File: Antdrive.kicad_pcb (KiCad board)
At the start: 2 copper layers, 29 x 32 mm, 27 parts, among them J1 Conn_01x06, J2 Conn_01x03, M1 Conn_01x02, M2 Conn_01x02, Q1 MMBT3904, U2 STM32F030F4Px, U3 DRV8848, U5 HT75xx-1-SOT89

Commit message: Fix auto reset circuits
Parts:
- removed mouse-bite-2mm-slot: VAL**, MountingEquipment:mouse-bite-2mm-slot
- C4: value 0.1u -> 2.2u
- R6: value 1k -> 680
- R7: value 1k -> 10k
- TP1, TP2, TP3: footprint TestPoint:TestPoint_Pad_D1.0mm -> TestPoint:TestPoint_Pad_D2.0mm
- moved TP2 3.32 mm to (158.0, 61.2)
- moved TP1 3.01 mm to (155.1, 61.2)
- moved G*** 0.14 mm to (163.4, 52.1)
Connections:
- C4 pad 1: DTR -> CTS
- R6 pad 1: DTR -> CTS
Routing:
- net DTR: track 20.9 -> 0.00 mm, vias 1 -> 0
- net CTS: track 28.1 -> 36.7 mm
- net BOOT: track 44.6 -> 51.1 mm
- net !RST: track 32.6 -> 33.9 mm
- net !SLEEP: track 34.1 -> 32.7 mm

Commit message: PCB updated
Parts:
- removed G***: LOGO, Symbol:lime_5mm
- removed TP3: Conn_01x01, TestPoint:TestPoint_Pad_D2.0mm
- added J3: Conn_01x03, Connector_PinHeader_2.54mm:PinHeader_1x03_P2.54mm_Vertical, F.Cu at (179.2, 55.2)
- added JP1: SolderJumper_3_Open, Jumper:SolderJumper-3_P1.3mm_Open_Pad1.0x1.5mm_NumberLabels, B.Cu at (176.5, 41.3)
- added JP2: SolderJumper_3_Open, Jumper:SolderJumper-3_P1.3mm_Open_Pad1.0x1.5mm_NumberLabels, B.Cu at (175.9, 54.6)
- added LOGO1: TestPoint, Symbol:lime_5mm, B.Cu at (161.2, 48.8)
- added U1: HT75xx-1-SOT89, Package_TO_SOT_SMD:SOT-89-3, F.Cu at (158.0, 53.6)
- moved BAT1 25.7 mm to (152.4, 46.6)
- moved R6 22.4 mm to (174.6, 53.5), turned to 0 degrees
- moved C4 21.2 mm to (174.6, 51.7)
- moved R4 18.0 mm to (175.6, 40.1), turned to 180 degrees
- moved TP2 16.7 mm to (171.6, 51.4)
- moved R7 16.3 mm to (171.3, 55.1)
- moved TP1 16.2 mm to (168.0, 51.4)
- moved C3 15.9 mm to (156.7, 40.0)
- moved J2 15.2 mm to (179.2, 40.5), turned to 0 degrees
- moved D1 15.1 mm to (174.9, 42.5), turned to 270 degrees
- moved D2 14.9 mm to (171.4, 53.5), turned to 0 degrees
- moved R3 14.7 mm to (167.9, 50.3)
- moved R1 13.7 mm to (171.3, 51.7), turned to 180 degrees
- moved C1 11.4 mm to (160.8, 50.8), turned to 180 degrees
- moved C2 11.3 mm to (159.4, 49.4), turned to 180 degrees
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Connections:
- J2 pad 2: +3V3 -> Net-(J2-Pad2)
- U2 pad 10: !SLEEP -> SERVO
- U2 pad 12: LED -> BIN1
- U2 pad 13: SERVO -> AIN1
- U2 pad 14: Net-(U2-Pad14) -> PPM
- U2 pad 19: PPM -> Net-(U2-Pad19)
- U2 pad 6: AIN1 -> LED
- U2 pad 7: AIN2 -> !SLEEP
- U2 pad 8: BIN2 -> AIN2
- U2 pad 9: BIN1 -> BIN2
- U3 pad 5: Net-(M2-Pad2) -> Net-(M2-Pad1)
- U3 pad 7: Net-(M2-Pad1) -> Net-(M2-Pad2)
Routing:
- net +BATT: track 24.4 -> 69.0 mm, vias 0 -> 3
- net +5V: track 0.00 -> 34.2 mm, vias 0 -> 2
- net BOOT: track 51.1 -> 20.6 mm, vias 5 -> 2
- net SERVO: track 39.4 -> 16.4 mm, vias 1 -> 2
- net !FAULT: track 31.2 -> 18.3 mm, vias 2 -> 0
- net !SLEEP: track 32.7 -> 43.9 mm, vias 2 -> 4
- net AIN1: track 8.31 -> 16.9 mm
- net LED: track 4.23 -> 10.9 mm, vias 0 -> 2
- net +3V3: track 71.3 -> 64.6 mm, vias 6 -> 4
- net RX: track 21.2 -> 14.7 mm
- net AIN2: track 8.31 -> 14.8 mm
- net CTS: track 36.7 -> 30.5 mm
- net BIN1: track 7.66 -> 12.8 mm, vias 2 -> 0
- net PPM: track 3.30 -> 7.53 mm
- net Net-(J3-Pad2): track 0.00 -> 4.09 mm
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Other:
- board size 29 x 32 mm -> 30 x 19.5 mm
- board text added: "-BAT+"
- board text added: "-M1+"
- board text added: "-M2+"
- board text added: "BAT/5V"
- board text added: "Ver 0.2"
- board text removed: "BAT+"
- board text removed: "BAT-"
- board text removed: "M1"
- board text removed: "M2"
- board text removed: "Ver 0.1"

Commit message: Update production files
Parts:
- removed LOGO1: TestPoint, Symbol:lime_5mm
- U1: value HT75xx-1-SOT89 -> AMS1117-5.0; footprint Package_TO_SOT_SMD:SOT-89-3 -> Package_TO_SOT_SMD:SOT-223-3_TabPin2
- moved C1 6.33 mm to (162.9, 56.8), turned to 0 degrees
- moved BAT1 2.15 mm to (150.3, 46.6)
- moved M1 2.15 mm to (150.3, 40.5)
- moved M2 2.15 mm to (150.3, 52.7)
- moved U1 1.15 mm to (157.0, 53.0)
- moved C2 0.90 mm to (160.0, 48.8), turned to 270 degrees
- moved JP2 0.63 mm to (176.5, 54.6)
- moved U5 0.13 mm to (163.7, 53.5)
- moved J2 0.05 mm to (179.2, 40.5)
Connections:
- U1 pad 2: +BATT -> +5V
- U1 pad 3: +5V -> +BATT
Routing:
- net +5V: track 34.2 -> 48.4 mm, vias 2 -> 3
- net !SLEEP: track 43.9 -> 48.6 mm
- net Net-(M1-Pad2): track 4.20 -> 6.60 mm
- net Net-(M1-Pad1): track 4.71 -> 7.11 mm
- net Net-(M2-Pad1): track 10.5 -> 12.4 mm
- net Net-(M2-Pad2): track 12.1 -> 13.4 mm
- net BIN1: track 12.8 -> 12.1 mm
- net Net-(J3-Pad2): track 4.09 -> 3.46 mm
- net GND: track 0.00 -> 0.13 mm, vias 5 -> 9
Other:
- board size 30 x 19.5 mm -> 32 x 20 mm

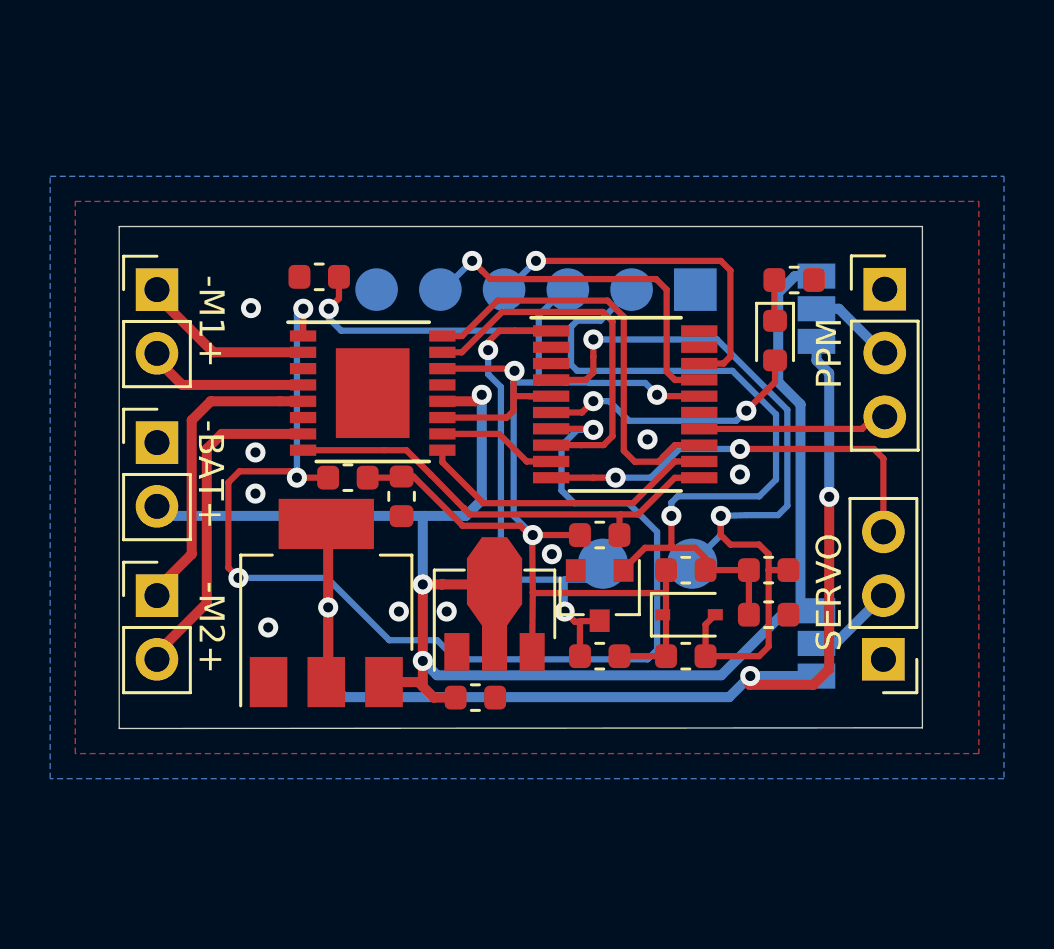
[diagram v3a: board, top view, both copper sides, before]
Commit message: Ver 0.3
Added config jumpers and hopefully fixed programming circuitry
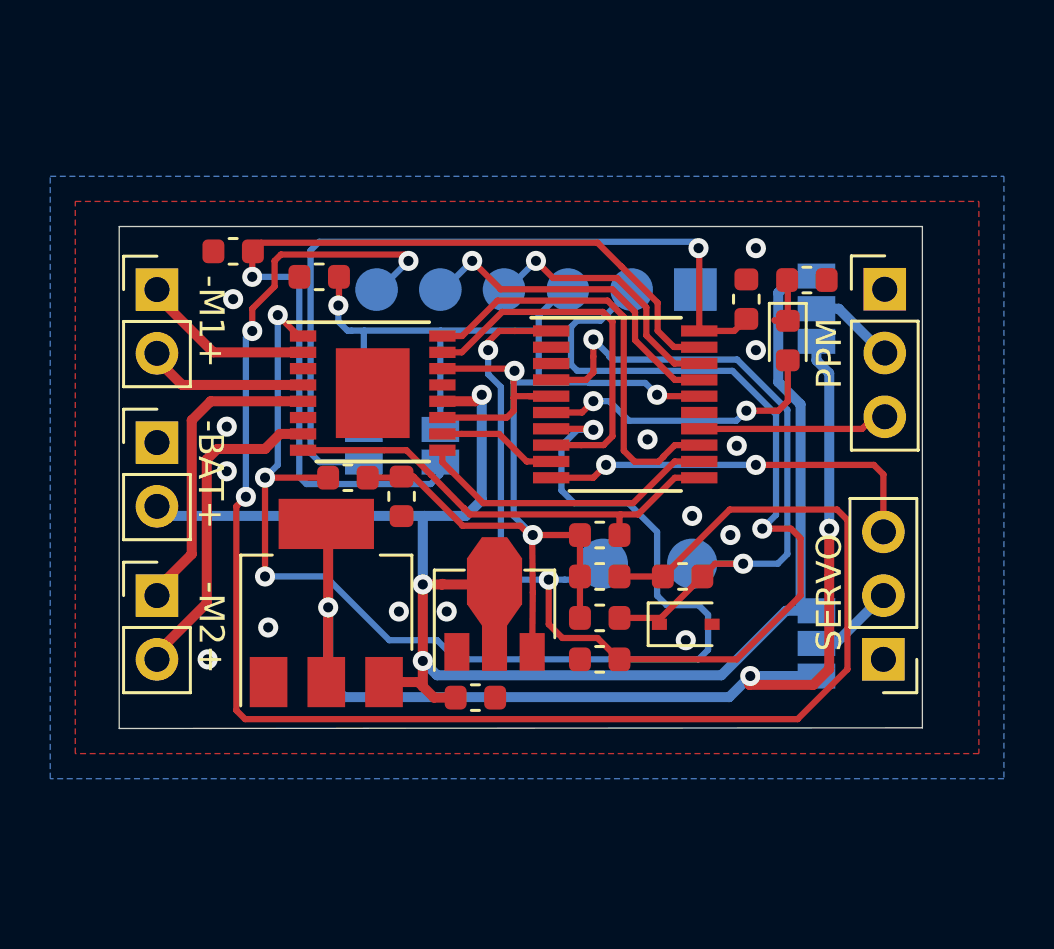
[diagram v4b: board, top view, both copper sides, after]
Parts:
- removed Q1: MMBT3904, Package_TO_SOT_SMD:SOT-23
- added JP3: SolderJumper_2_Open, Jumper:SolderJumper-2_P1.3mm_Open_Pad1.0x1.5mm, B.Cu at (161.5, 46.7)
- added JP4: SolderJumper_2_Open, Jumper:SolderJumper-2_P1.3mm_Open_Pad1.0x1.5mm, B.Cu at (158.5, 46.7)
- added R8: 1k, Resistor_SMD:R_0603_1608Metric, F.Cu at (167.9, 51.9)
- R6: value 680 -> 1k
- moved R1 22.1 mm to (153.3, 39.0), turned to 0 degrees
- moved R6 12.6 mm to (173.7, 40.9), turned to 270 degrees
- moved R7 3.75 mm to (167.9, 53.6)
- moved C4 3.44 mm to (171.2, 51.9)
- moved D1 0.51 mm to (175.4, 42.5)
- moved R4 0.51 mm to (176.1, 40.1)
- moved D2 0.40 mm to (171.3, 53.8)
- moved R5 0.13 mm to (167.9, 55.2)
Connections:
- C4 pad 1: CTS -> DTR
- D2 pad 1: +3V3 -> !RST
- D2 pad 2: !RST -> GND
- J1 pad 2: CTS -> BOOT
- R1 pad 1: CTS -> GND
- R1 pad 2: +3V3 -> CFG1
- R5 pad 1: BOOT -> GND
- R5 pad 2: +3V3 -> BOOT
- R6 pad 1: CTS -> GND
- R6 pad 2: GND -> CFG2
- U2 pad 19: Net-(U2-Pad19) -> CFG1
- U2 pad 20: Net-(U2-Pad20) -> CFG2
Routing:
- net DTR: track 0.00 -> 67.5 mm, vias 0 -> 3
- net CFG1: track 0.00 -> 37.4 mm, vias 0 -> 1
- net CFG2: track 0.00 -> 32.2 mm, vias 0 -> 1
- net BOOT: track 20.6 -> 52.1 mm, vias 2 -> 3
- net CTS: track 30.5 -> 0.00 mm, vias 1 -> 0
- net !RST: track 33.0 -> 27.8 mm
- net TX: track 14.4 -> 10.6 mm
- net RX: track 14.7 -> 13.4 mm
- net LED: track 10.9 -> 11.9 mm
- net !SLEEP: track 48.6 -> 49.2 mm
- net GND: vias 9 -> 14
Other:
- board text added: "15/06/2020"
- board text added: "CFG1"
- board text added: "CFG2"
- board text added: "Ver 0.3"
- board text removed: "21/04/2020"
- board text removed: "Ver 0.2"

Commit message: Added documentation
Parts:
- R5: value 1k -> 100k
- moved D1 1.91 mm to (175.4, 44.5)
- moved R4 1.08 mm to (175.4, 40.9), turned to 270 degrees
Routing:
- net LED: track 11.9 -> 10.1 mm
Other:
- board text added: "14/07/2020"
- board text added: "RECEIVER"
- board text added: "Ver 1.0"
- board text removed: "15/06/2020"
- board text removed: "PPM"
- board text removed: "Ver 0.3"
